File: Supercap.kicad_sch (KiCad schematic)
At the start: 3 parts

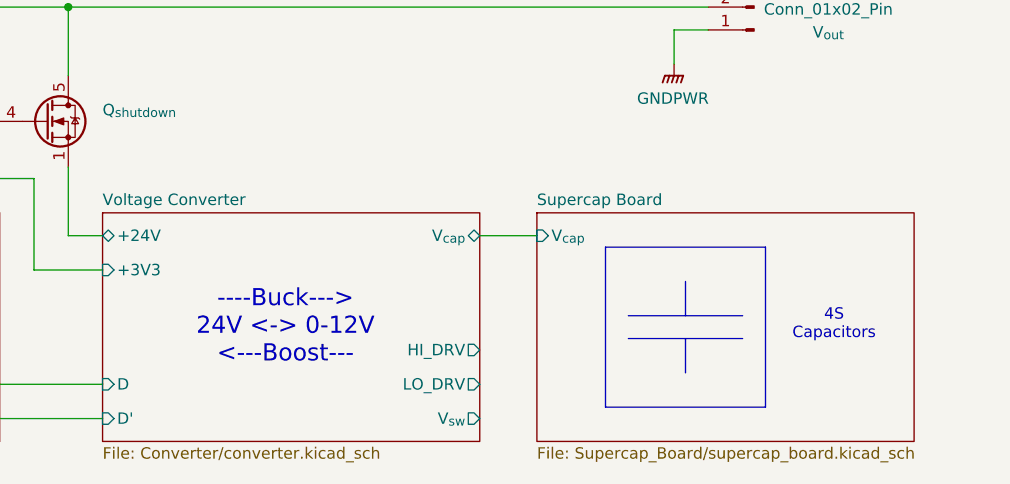
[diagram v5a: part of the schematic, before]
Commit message: changed converter topology to full-bridge design
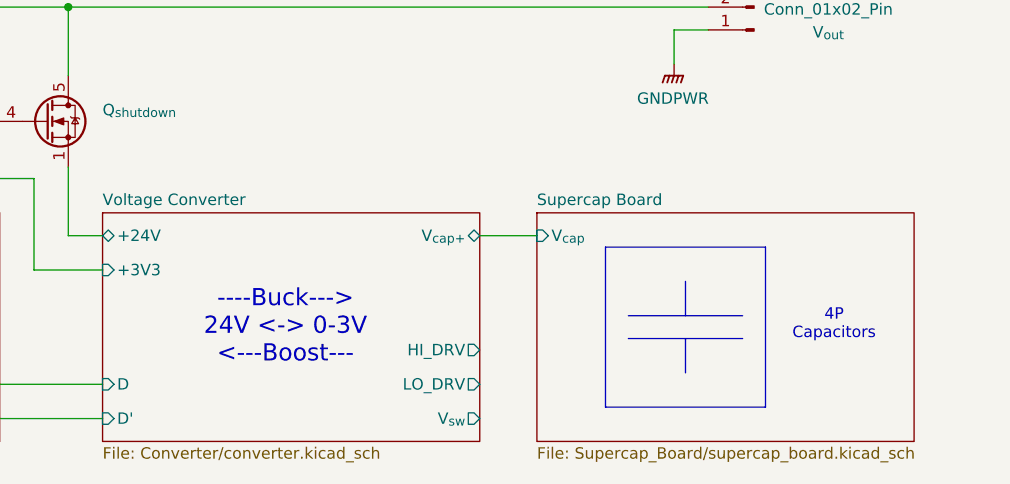
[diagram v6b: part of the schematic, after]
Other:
- sheet Voltage Converter ports: added V_{cap+}; removed V_{cap}
- note added: "----Buck---> 24V <-> 0-3V <---Boost---"
- note added: "4P Capacitors"
- note removed: "----Buck---> 24V <-> 0-12V <---Boost---"
- note removed: "4S Capacitors"
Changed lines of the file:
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@@
 		)
 	)
-	(text "----Buck--->\n24V <-> 0-12V\n<---Boost---"
+	(text "----Buck--->\n24V <-> 0-3V\n<---Boost---"
 		(exclude_from_sim no)
 		(at 162.56 90.17 0)
@@
 		)
 	)
-	(text "4S\nCapacitors"
+	(text "4P\nCapacitors"
 		(exclude_from_sim no)
 		(at 223.52 89.916 0)
@@
 			)
 		)
-		(pin "V_{cap}" bidirectional
+		(pin "V_{cap+}" bidirectional
 			(at 184.15 80.01 0)
 			(effects

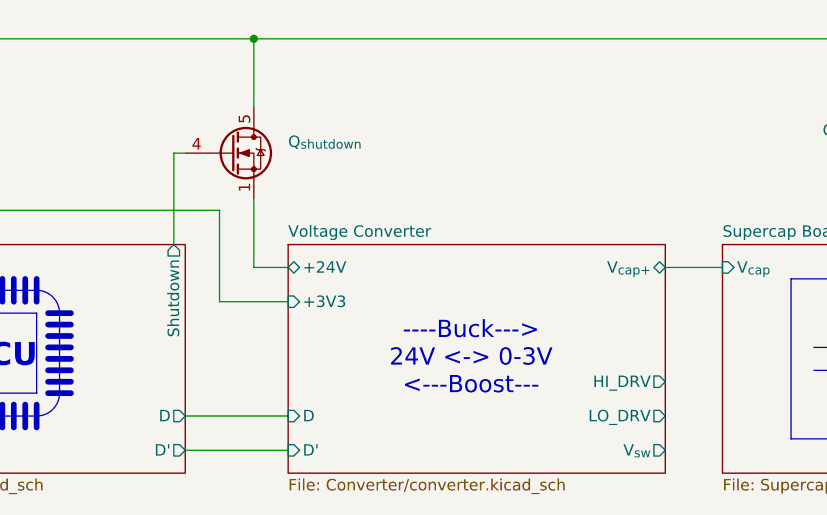
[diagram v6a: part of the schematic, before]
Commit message: added symbol libraries and finished gate driver circuitry schematic
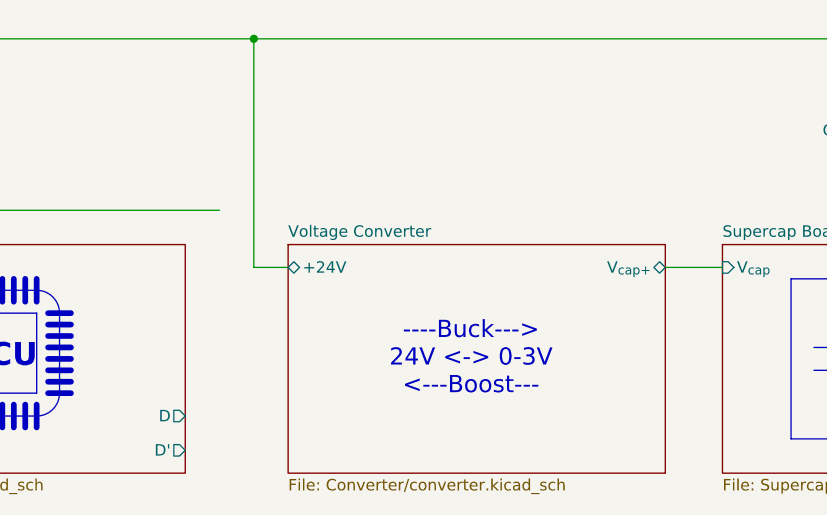
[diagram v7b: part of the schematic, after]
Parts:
- removed Q_{shutdown}: ~, symbol Transistor_FET:FDMS8350LET40
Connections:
- net Voltage Converter/+24V: now also V_{in}.1 (Pin_1), V_{out}.2 (Pin_2)
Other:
- sheet Control ports: added none; removed Shutdown
- sheet Voltage Converter ports: added none; removed +3V3, D, D', HI_DRV, LO_DRV, V_{sw}
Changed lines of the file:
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@@
 		(color 0 0 0 0)
 	)
-	(wire
-		(pts
-			(xy 134.62 83.82) (xy 134.62 73.66)
-		)
-		(stroke
-			(width 0)
-			(type default)
-		)
-	)
 	(polyline
 		(pts
@@
 	(wire
 		(pts
-			(xy 138.43 54.61) (xy 138.43 62.23)
-		)
-		(stroke
-			(width 0)
-			(type default)
-		)
-	)
-	(wire
-		(pts
-			(xy 130.81 100.33) (xy 142.24 100.33)
+			(xy 138.43 54.61) (xy 138.43 80.01)
 		)
 		(stroke
@@
 		)
 	)
-	(wire
-		(pts
-			(xy 130.81 67.31) (xy 129.54 67.31)
-		)
-		(stroke
-			(width 0)
-			(type default)
-		)
-	)
 	(polyline
 		(pts
@@
 		)
 	)
-	(wire
-		(pts
-			(xy 129.54 67.31) (xy 129.54 77.47)
-		)
-		(stroke
-			(width 0)
-			(type default)
-		)
-	)
-	(wire
-		(pts
-			(xy 130.81 96.52) (xy 142.24 96.52)
-		)
-		(stroke
-			(width 0)
-			(type default)
-		)
-	)
 	(polyline
 		(pts
@@
 		)
 	)
-	(wire
-		(pts
-			(xy 138.43 72.39) (xy 138.43 80.01)
-		)
-		(stroke
-			(width 0)
-			(type default)
-		)
-	)
 	(polyline
 		(pts
@@
 		(pts
 			(xy 138.43 54.61) (xy 209.55 54.61)
-		)
-		(stroke
-			(width 0)
-			(type default)
-		)
-	)
-	(wire
-		(pts
-			(xy 142.24 83.82) (xy 134.62 83.82)
 		)
 		(stroke
@@
 		)
 	)
-	(symbol
-		(lib_id "Transistor_FET:FDMS8350LET40")
-		(at 135.89 67.31 0)
-		(unit 1)
-		(exclude_from_sim no)
-		(in_bom yes)
-		(on_board yes)
-		(dnp no)
-		(fields_autoplaced yes)
-		(property "Reference" "Q_{shutdown}"
-			(at 142.24 66.0399 0)
-			(effects
-				(font
-					(size 1.27 1.27)
-				)
-				(justify left)
-			)
-		)
-		(property "Value" "~"
-			(at 142.24 68.5799 0)
-			(effects
-				(font
-					(size 1.27 1.27)
-				)
-				(justify left)
-			)
-		)
-		(property "Footprint" ""
-			(at 140.97 69.215 0)
-			(effects
-				(font
-					(size 1.27 1.27)
-					(italic yes)
-				)
-				(justify left)
-				(hide yes)
-			)
-		)
-		(property "Datasheet" ""
-			(at 140.97 71.12 0)
-			(effects
-				(font
-					(size 1.27 1.27)
-				)
-				(justify left)
-				(hide yes)
-			)
-		)
-		(property "Description" ""
-			(at 135.89 67.31 0)
-			(effects
-				(font
-					(size 1.27 1.27)
-				)
-				(hide yes)
-			)
-		)
-		(pin "4"
-		)
-		(pin "2"
-		)
-		(pin "5"
-		)
-		(pin "1"
-		)
-		(pin "3"
-		)
-		(instances
-			(project ""
-				(path "/98ee8313-37ab-4329-91ab-b5710476f82f"
-					(reference "Q_{shutdown}")
-					(unit 1)
-				)
-			)
-		)
-	)
 	(sheet
 		(at 40.64 77.47)
@@
 			)
 		)
-		(pin "+3V3" input
-			(at 142.24 83.82 180)
-			(effects
-				(font
-					(size 1.27 1.27)
-				)
-				(justify left)
-			)
-		)
 		(pin "V_{cap+}" bidirectional
 			(at 184.15 80.01 0)
@@
 			)
 		)
-		(pin "V_{sw}" output
-			(at 184.15 100.33 0)
-			(effects
-				(font
-					(size 1.27 1.27)
-				)
-				(justify right)
-			)
-		)
 		(pin "+24V" bidirectional
 			(at 142.24 80.01 180)
@@
 				)
 				(justify left)
-			)
-		)
-		(pin "HI_DRV" output
-			(at 184.15 92.71 0)
-			(effects
-				(font
-					(size 1.27 1.27)
-				)
-				(justify right)
-			)
-		)
-		(pin "D'" input
-			(at 142.24 100.33 180)
-			(effects
-				(font
-					(size 1.27 1.27)
-				)
-				(justify left)
-			)
-		)
-		(pin "D" input
-			(at 142.24 96.52 180)
-			(effects
-				(font
-					(size 1.27 1.27)
-				)
-				(justify left)
-			)
-		)
-		(pin "LO_DRV" output
-			(at 184.15 96.52 0)
-			(effects
-				(font
-					(size 1.27 1.27)
-				)
-				(justify right)
 			)
 		)
@@
 			(effects
 				(font
-					(size 1.27 1.27)
-				)
-				(justify right)
-			)
-		)
-		(pin "Shutdown" output
-			(at 129.54 77.47 90)
-			(effects
-				(font

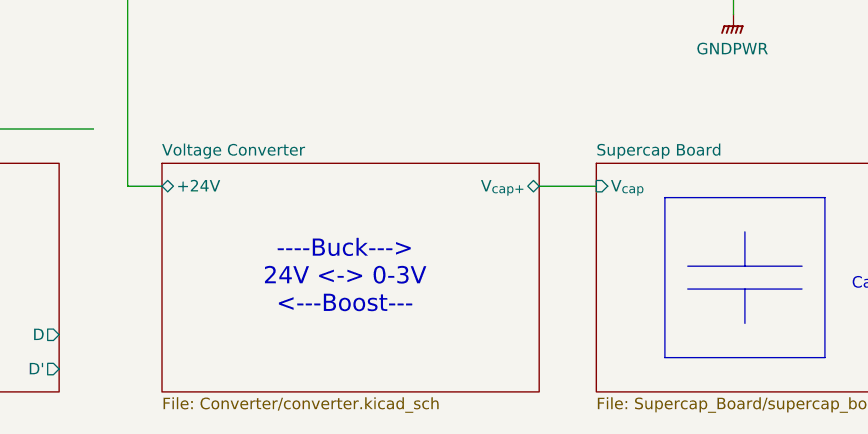
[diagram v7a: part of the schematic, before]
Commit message: fixed converter section
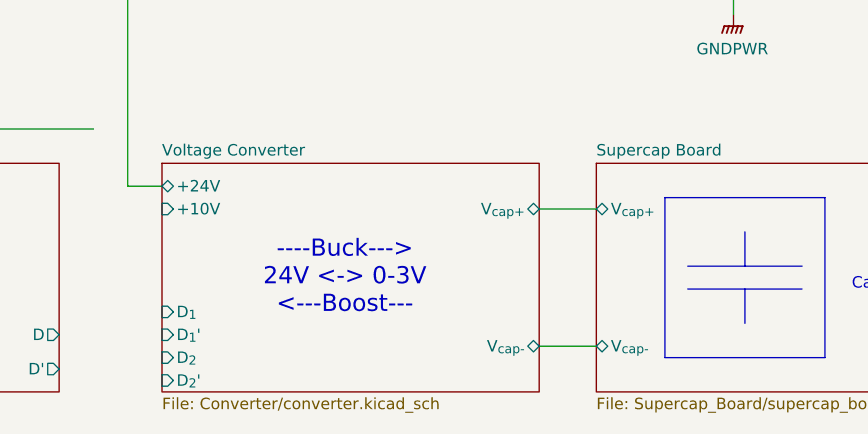
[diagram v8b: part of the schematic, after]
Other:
- sheet Supercap Board ports: added V_{cap+}, V_{cap-}; removed V_{cap}
- sheet Voltage Converter ports: added +10V, D_{1}, D_{1}', D_{2}, D_{2}', V_{cap-}; removed none
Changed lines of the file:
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@@
-		)
-	)
-	(wire
-		(pts
-			(xy 184.15 80.01) (xy 190.5 80.01)
-		)
-		(stroke
-			(width 0)
-			(type default)
 		)
 	)
@@
 	(wire
 		(pts
+			(xy 184.15 97.79) (xy 190.5 97.79)
+		)
+		(stroke
+			(width 0)
+			(type default)
+		)
+	)
+	(wire
+		(pts
 			(xy 134.62 73.66) (xy 86.36 73.66)
 		)
@@
 			(width 0.635)
 			(type solid)
+		)
+	)
+	(wire
+		(pts
+			(xy 184.15 82.55) (xy 190.5 82.55)
+		)
+		(stroke
+			(width 0)
+			(type default)
 		)
 	)
@@
 		)
 		(pin "V_{cap+}" bidirectional
-			(at 184.15 80.01 0)
+			(at 184.15 82.55 0)
 			(effects
 				(font
@@
 				)
 				(justify left)
+			)
+		)
+		(pin "+10V" input
+			(at 142.24 82.55 180)
+			(effects
+				(font
+					(size 1.27 1.27)
+				)
+				(justify left)
+			)
+		)
+		(pin "D_{1}" input
+			(at 142.24 93.98 180)
+			(effects
+				(font
+					(size 1.27 1.27)
+				)
+				(justify left)
+			)
+		)
+		(pin "D_{1}'" input
+			(at 142.24 96.52 180)
+			(effects
+				(font
+					(size 1.27 1.27)
+				)
+				(justify left)
+			)
+		)
+		(pin "D_{2}" input
+			(at 142.24 99.06 180)
+			(effects
+				(font
+					(size 1.27 1.27)
+				)
+				(justify left)
+			)
+		)
+		(pin "D_{2}'" input
+			(at 142.24 101.6 180)
+			(effects
+				(font
+					(size 1.27 1.27)
+				)
+				(justify left)
+			)
+		)
+		(pin "V_{cap-}" bidirectional
+			(at 184.15 97.79 0)
+			(effects
+				(font
+					(size 1.27 1.27)
+				)
+				(justify right)
 			)
 		)
@@
 			)
 		)
-		(pin "V_{cap}" input
-			(at 190.5 80.01 180)
-			(effects
-				(font
+		(pin "V_{cap+}" bidirectional
+			(at 190.5 82.55 180)
+			(effects
+				(font
+					(size 1.27 1.27)
+				)
+				(justify left)
+			)
+		)
+		(pin "V_{cap-}" bidirectional
+			(at 190.5 97.79 180)
+			(effects
+				(font
